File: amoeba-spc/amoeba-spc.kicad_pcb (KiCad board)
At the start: 2 copper layers, 38.9 x 16.1 mm, 17 parts

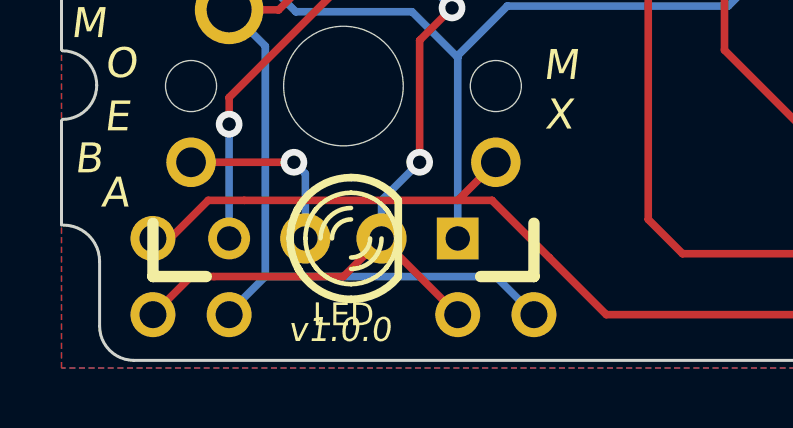
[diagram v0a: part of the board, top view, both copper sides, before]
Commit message: Fixes for Oshpark submission and minor labeling adjustments.
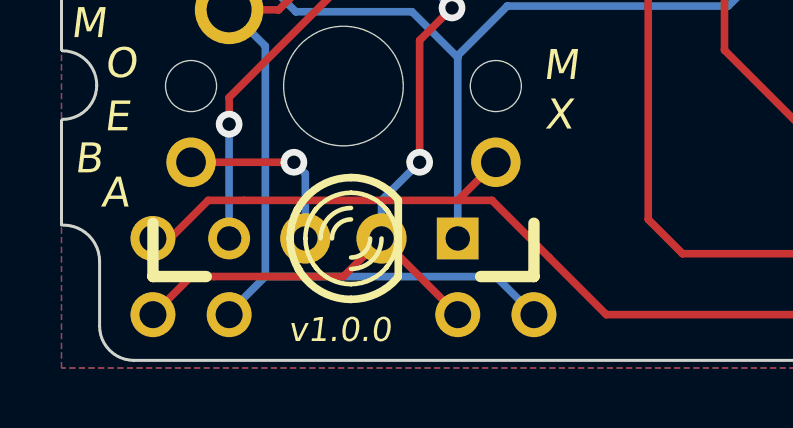
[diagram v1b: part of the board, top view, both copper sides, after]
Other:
- board text added: "Amoeba MX SPC v1.0.0"
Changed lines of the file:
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@@
     (area 226.771288 96.874 284.480001 141.003)
     (thickness 1.6)
-    (drawings 83)
+    (drawings 77)
     (tracks 60)
     (zones 0)
@@
   (page A3)
   (layers
-    (15 F.Cu signal)
-    (0 B.Cu signal)
-    (16 B.Adhes user)
-    (17 F.Adhes user)
-    (18 B.Paste user)
-    (19 F.Paste user)
+    (15 F.Cu signal hide)
+    (0 B.Cu signal hide)
+    (16 B.Adhes user hide)
+    (17 F.Adhes user hide)
+    (18 B.Paste user hide)
+    (19 F.Paste user hide)
     (20 B.SilkS user)
     (21 F.SilkS user)
@@
       (effects (font (size 1.27 1.016) (thickness 0.2032)) (justify mirror))
     )
-    (fp_text value RESISTOR (at 0 0) (layer B.SilkS) hide
-      (effects (font (size 1.27 1.016) (thickness 0.2032)) (justify mirror))
+    (fp_text value RESISTOR (at 0 0) (layer B.SilkS)
+      (effects (font (size 0.8 0.8) (thickness 0.2)) (justify mirror))
     )
     (fp_line (start -3.175 1.27) (end 3.175 1.27) (layer Dwgs.User) (width 0.381))
@@
       (effects (font (size 0.762 0.762) (thickness 0.0889)))
     )
-    (fp_text value LED (at 0 2.54) (layer F.SilkS)
+    (fp_text value LED (at 0 2.54) (layer F.SilkS) hide
       (effects (font (size 0.762 0.762) (thickness 0.0889)))
     )
@@
     )
   )
+  (gr_line (start 249.1359 107.4166) (end 249.1359 105.7021) (angle 90) (layer B.SilkS) (width 0.2))
   (gr_line (start 275.0185 106.7435) (end 272.9865 106.7435) (angle 90) (layer B.SilkS) (width 0.2))
   (gr_text GND (at 261.874 107.188) (layer B.SilkS)
@@
     (arrow2b (pts (xy 248.92 132.079999) (xy 250.046503 131.493579)))
   )
-  (gr_text O (at 253.365 108.5215) (layer B.SilkS)
-    (effects (font (size 1 1) (thickness 0.25) italic) (justify mirror))
-  )
-  (gr_text M (at 254.889 108.839) (layer B.SilkS)
-    (effects (font (size 1 1) (thickness 0.25) italic) (justify mirror))
-  )
-  (gr_text A (at 249.6185 107.5055) (layer B.SilkS)
-    (effects (font (size 1 1) (thickness 0.25) italic) (justify mirror))
-  )
-  (gr_text A (at 256.159 109.728) (layer B.SilkS)
-    (effects (font (size 1 1) (thickness 0.25) italic) (justify mirror))
-  )
-  (gr_text E (at 252.1585 109.093) (layer B.SilkS)
-    (effects (font (size 1 1) (thickness 0.25) italic) (justify mirror))
-  )
-  (gr_text B (at 250.952 108.331) (layer B.SilkS)
-    (effects (font (size 1 1) (thickness 0.25) italic) (justify mirror))
-  )
-  (gr_text v1.0.0 (at 255.524 105.283) (layer B.SilkS)
-    (effects (font (size 0.8 0.8) (thickness 0.2) italic) (justify mirror))
+  (gr_text "Amoeba MX\nSPC\nv1.0.0" (at 264.7188 111.2139) (layer B.SilkS)
+    (effects (font (size 1 1) (thickness 0.125) italic) (justify mirror))
   )
   (gr_line (start 250.19 116.078) (end 250.19 117.348) (angle 90) (layer B.SilkS) (width 0.1))
@@
   (gr_line (start 247.5865 117.7925) (end 245.11 117.7925) (angle 90) (layer B.SilkS) (width 0.2))
   (gr_line (start 249.2375 117.0305) (end 249.2375 118.364) (angle 90) (layer B.SilkS) (width 0.2))
-  (gr_line (start 248.3485 107.061) (end 248.3485 105.41) (angle 90) (layer B.SilkS) (width 0.1))
   (gr_line (start 256.8575 117.475) (end 255.27 117.475) (angle 90) (layer B.SilkS) (width 0.2))
   (gr_line (start 241.046 117.475) (end 242.57 117.475) (angle 90) (layer B.SilkS) (width 0.2))
@@
     (effects (font (size 0.8 0.8) (thickness 0.2)) (justify left mirror))
   )
-  (gr_text SC (at 248.2215 106.807) (layer B.SilkS)
-    (effects (font (size 0.6 0.6) (thickness 0.15)) (justify left mirror))
+  (gr_text SC (at 248.8946 107.1118) (layer B.SilkS)
+    (effects (font (size 0.8 0.8) (thickness 0.15)) (justify left mirror))
   )
   (gr_text SC (at 256.9845 116.9035) (layer B.SilkS)
